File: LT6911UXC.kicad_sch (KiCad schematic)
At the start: 38 parts, among them U7 TC358743XBG_EL_NOK, U8 LX7167ACLD-TR, U9 TLV62568DBVR, X2 27MHz

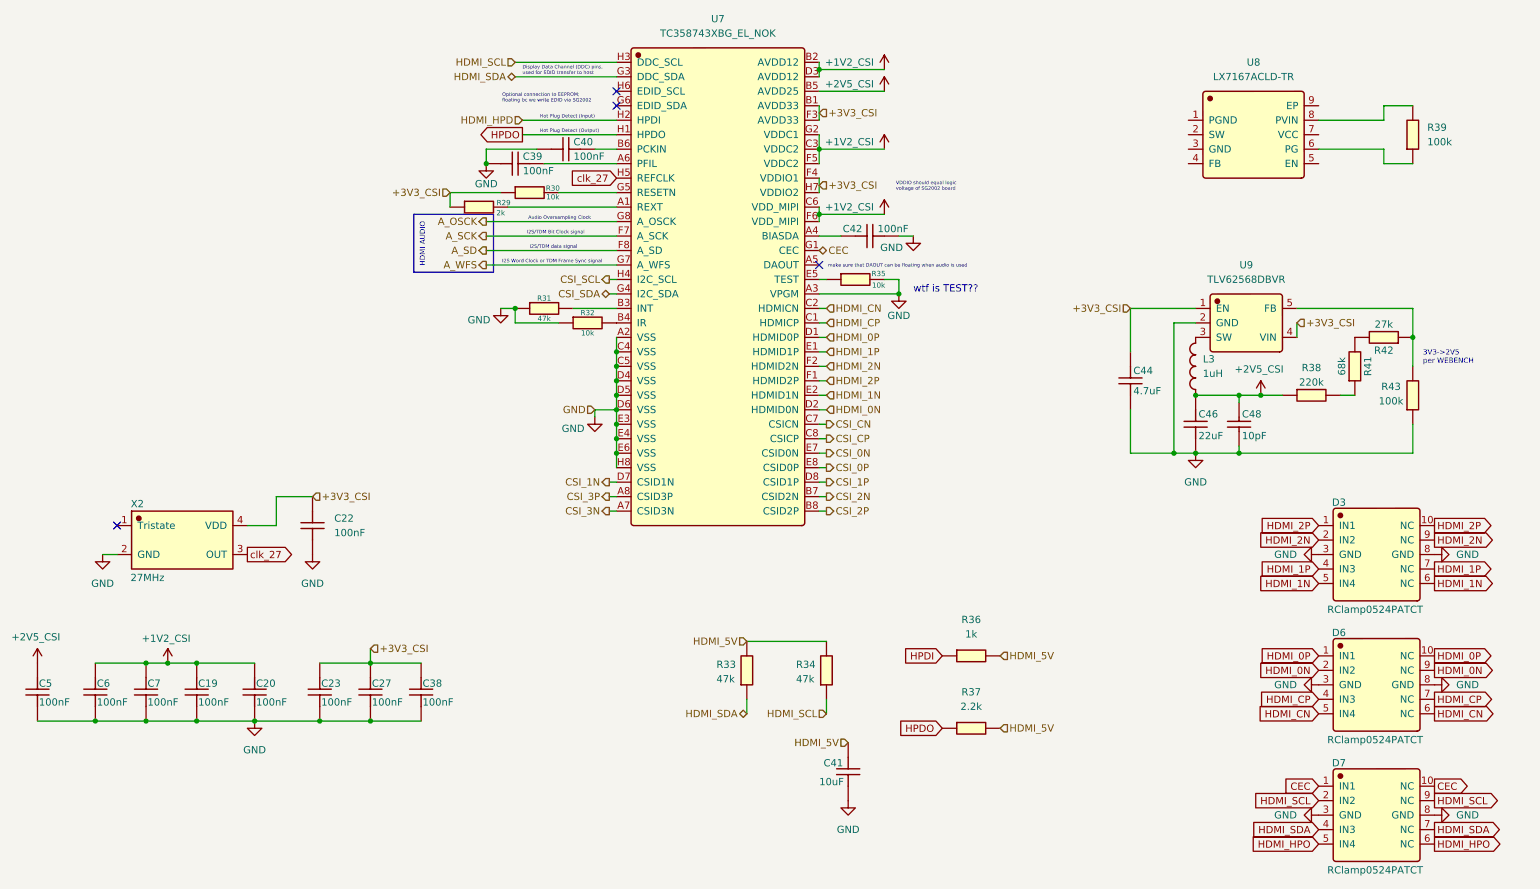
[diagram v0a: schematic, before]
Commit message: Cleaned up schematic and replaced TC358743XBG with reverse-engineered LT6911C
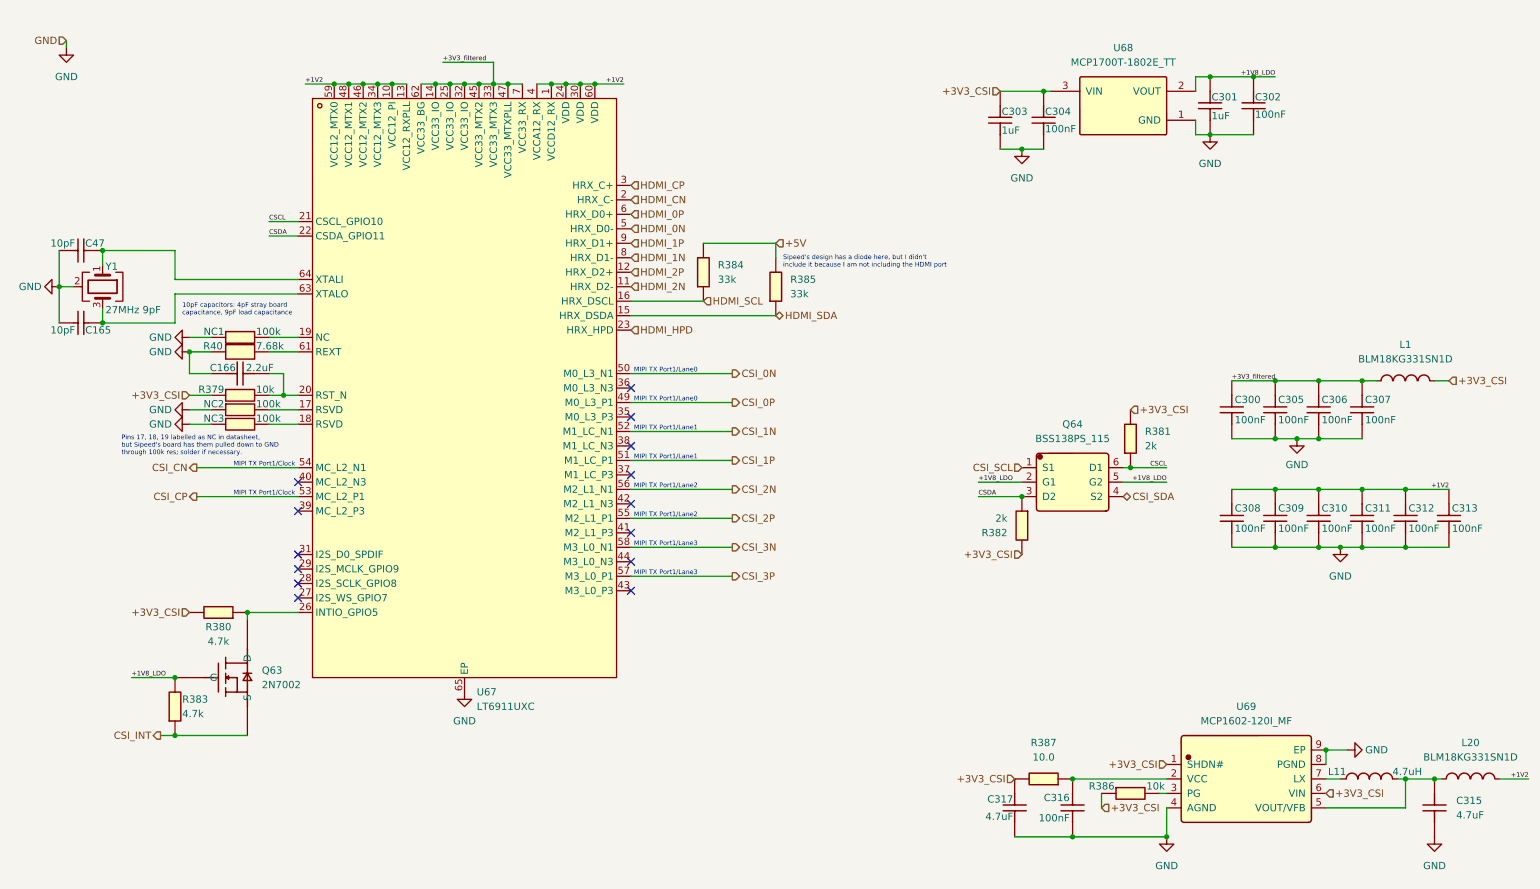
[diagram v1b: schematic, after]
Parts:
- removed C19, C20, C22, C23, C27, C38, C39, C40, C42, C5, C6, C7: 100nF, Capacitor_SMD:C_0402_1005Metric, symbol JLCImport:CL05B104KB54PNC
- removed C41: 10uF, Capacitor_SMD:C_0603_1608Metric, symbol JLCImport:CL10A106KP8NNNC
- removed C44: 4.7uF, Capacitor_SMD:C_0603_1608Metric, symbol JLCImport:CL10A475KO8NNNC
- removed C46: 22uF, Capacitor_SMD:C_0603_1608Metric, symbol JLCImport:CL10A226MQ8NRNC
- removed C48: 10pF, Capacitor_SMD:C_0603_1608Metric, symbol JLCImport:CL10C100JB8NNNC
- removed D3, D6, D7: RClamp0524PATCT, JLCImport:RClamp0524PATCT, symbol JLCImport:RClamp0524PATCT
- removed L3: 1uH, TerminalBlock_Phoenix:TerminalBlock_Phoenix_PTSM-0,5-2-2,5-V-SMD_1x02-1MP_P2.50mm_Vertical, symbol JLCImport:FTC252012S1R0MBCA
- removed R29: 2k, Resistor_SMD:R_0603_1608Metric, symbol JLCImport:0603WAF2001T5E
- removed R30, R32, R35: 10k, Resistor_SMD:R_0402_1005Metric, symbol JLCImport:0402WGF1002TCE
- removed R31, R33, R34: 47k, Resistor_SMD:R_0402_1005Metric, symbol JLCImport:0402WGF4702TCE
- removed R36: 1k, Resistor_SMD:R_0402_1005Metric, symbol JLCImport:0402WGF1001TCE
- removed R37: 2.2k, Resistor_SMD:R_0402_1005Metric, symbol JLCImport:0402WGF2201TCE
- removed R38: 220k, Resistor_SMD:R_0603_1608Metric, symbol JLCImport:0603WAF2203T5E
- removed R39, R43: 100k, Resistor_SMD:R_0402_1005Metric, symbol JLCImport:0402WGF1003TCE
- removed R41: 68k, Resistor_SMD:R_0603_1608Metric, symbol JLCImport:0603WAF6802T5E
- removed R42: 27k, Resistor_SMD:R_0603_1608Metric, symbol JLCImport:0603WAF2702T5E
- removed U7: TC358743XBG_EL_NOK, JLCImport:TC358743XBG_EL_NOK, symbol JLCImport:TC358743XBG_EL_NOK
- removed U8: LX7167ACLD-TR, JLCImport:LX7167ACLD-TR, symbol JLCImport:LX7167ACLD-TR
- removed U9: TLV62568DBVR, JLCImport:TLV62568DBVR, symbol JLCImport:TLV62568DBVR
- removed X2: 27MHz, Oscillator:Oscillator_SMD_Silicon_Labs_LGA-6_2.5x3.2mm_P1.25mm, symbol JLCImport:XOS32027000LT00351005
- added C165, C47: 10pF, Capacitor_SMD:C_0603_1608Metric, symbol JLCImport:CL10C100JB8NNNC
- added C166: 2.2uF, Capacitor_SMD:C_0402_1005Metric, symbol JLCImport:JMK105BJ225MVHF
- added C300, C302, C304, C305, C306, C307, C308, C309, C310, C311, C312, C313, C316: 100nF, Capacitor_SMD:C_0402_1005Metric, symbol JLCImport:CL05B104KB54PNC
- added C301, C303: 1uF, Capacitor_SMD:C_0402_1005Metric, symbol JLCImport:CL05A105KA5NQNC
- added C315, C317: 4.7uF, Capacitor_SMD:C_0402_1005Metric, symbol JLCImport:CL05A475MP5NRNC
- added L1, L20: BLM18KG331SN1D, JLCImport:BLM18KG331SN1D, symbol JLCImport:BLM18KG331SN1D
- added L11: 4.7uH, JLCImport:PIM201608S4R7MBCA, symbol JLCImport:PIM201608S4R7MBCA
- added NC1, NC2, NC3: 100k, Resistor_SMD:R_0402_1005Metric, symbol JLCImport:0402WGF1003TCE
- added Q63: 2N7002, JLCImport:2N7002_C916396, symbol JLCImport:2N7002_C916396
- added Q64: BSS138PS_115, JLCImport:BSS138PS_115, symbol JLCImport:BSS138PS_115
- added R379, R386: 10k, Resistor_SMD:R_0402_1005Metric, symbol JLCImport:0402WGF1002TCE
- added R380, R383: 4.7k, Resistor_SMD:R_0402_1005Metric, symbol JLCImport:0402WGF4701TCE
- added R381, R382: 2k, Resistor_SMD:R_0603_1608Metric, symbol JLCImport:0603WAF2001T5E
- added R384, R385: 33k, Resistor_SMD:R_0402_1005Metric, symbol JLCImport:WR04X3302FTL
- added R387: 10.0, Resistor_SMD:R_0402_1005Metric, symbol JLCImport:0402WGF100JTCE
- added R40: 7.68k, Resistor_SMD:R_0402_1005Metric, symbol JLCImport:CL0402FN7K68P
- added U67: LT6911UXC, LT6911UXC:QFN-64_L7.5-W7.5-P0.40-TL-EP6.2, symbol LT6911UXC:LT6911UXC
- added U68: MCP1700T-1802E_TT, JLCImport:MCP1700T-1802E_TT, symbol JLCImport:MCP1700T-1802E_TT
- added U69: MCP1602-120I_MF, JLCImport:MCP1602-120I_MF, symbol JLCImport:MCP1602-120I_MF
- added Y1: 27MHz 9pF, Crystal:Crystal_SMD_3225-4Pin_3.2x2.5mm, symbol Device:Crystal_GND24
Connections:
- net +3V3_CSI: now also C303.2, C304.2, C317.2, L1.2, R379.1, R380.2, R381.2, R382.2, R386.1, R387.2, U68.3 (VIN), U69.1 (SHDN#), U69.6 (VIN)
- net CSI_0N: now also U67.50 (M0_L3_N1)
- net CSI_0P: now also U67.49 (M0_L3_P1)
- net CSI_1N: now also U67.52 (M1_LC_N1)
- net CSI_1P: now also U67.51 (M1_LC_P1)
- net CSI_2N: now also U67.56 (M2_L1_N1)
- net CSI_2P: now also U67.55 (M2_L1_P1)
- net CSI_3N: now also U67.58 (M3_L0_N1)
- net CSI_3P: now also U67.57 (M3_L0_P1)
- net CSI_CN: now also U67.54 (MC_L2_N1)
- net CSI_CP: now also U67.53 (MC_L2_P1)
- net CSI_SCL: now also Q64.1 (S1)
- net CSI_SDA: now also Q64.4 (S2)
- net GND: now also C165.2, C166.2, C300.1, C301.1, C302.1, C303.1, C304.1, C305.1, C306.1, C307.1, C308.1, C309.1, C310.1, C311.1, C312.1, C313.1, C315.1, C316.1, C317.1, C47.1, NC1.1, NC2.1, NC3.1, R40.1, U67.65 (EP), U68.1 (GND), U69.4 (AGND), U69.8 (PGND), U69.9 (EP), Y1.2 (G), Y1.4 (G)
- net HDMI_0N: now also U67.5 (HRX_D0-)
- net HDMI_0P: now also U67.6 (HRX_D0+)
- net HDMI_1N: now also U67.8 (HRX_D1-)
- net HDMI_1P: now also U67.9 (HRX_D1+)
- net HDMI_2N: now also U67.11 (HRX_D2-)
- net HDMI_2P: now also U67.12 (HRX_D2+)
- net HDMI_CN: now also U67.2 (HRX_C-)
- net HDMI_CP: now also U67.3 (HRX_C+)
- net HDMI_HPD: now also U67.23 (HRX_HPD)
- net HDMI_SCL: now also R384.1, U67.16 (HRX_DSCL)
- net HDMI_SDA: now also R385.1, U67.15 (HRX_DSDA)
- new net: C47.2, U67.64 (XTALI), Y1.1
- new net: C316.2, R387.1, U69.2 (VCC)
- new net: R386.2, U69.3 (PG)
- new net: C315.2, L11.2, L20.1, U69.5 (VOUT/VFB)
- new net: L11.1, U69.7 (LX)
- new net: Q63.3 (D), R380.1, U67.26 (INTIO_GPIO5)
- new net: C165.1, U67.63 (XTALO), Y1.3
- new net: NC2.2, U67.17 (RSVD)
- new net: NC3.2, U67.18 (RSVD)
- new net: NC1.2, U67.19 (NC)
- new net: C166.1, R379.2, U67.20 (RST_N)
- new net: R40.2, U67.61 (REXT)
- new net +1V2: C308.2, C309.2, C310.2, C311.2, C312.2, C313.2, L20.2, U67.1 (VCCD12_RX), U67.10 (VCC12_PI), U67.13 (VCC12_RXPLL), U67.24 (VDD), U67.30 (VDD), U67.34 (VCC12_MTX3), U67.4 (VCCA12_RX), U67.46 (VCC12_MTX2), U67.48 (VCC12_MTX1), U67.59 (VCC12_MTX0), U67.60 (VDD)
- new net +1V8_LDO: C301.2, C302.2, Q63.1 (G), Q64.2 (G1), Q64.5 (G2), R383.2, U68.2 (VOUT)
- new net +3V3_filtered: C300.2, C305.2, C306.2, C307.2, L1.1, U67.14 (VCC33_IO), U67.25 (VCC33_IO), U67.32 (VCC33_IO), U67.33 (VCC33_MTX3), U67.45 (VCC33_MTX2), U67.47 (VCC33_MTXPLL), U67.62 (VCC33_BG), U67.7 (VCC33_RX)
- new net +5V: R384.2, R385.2
- new net CSCL: Q64.6 (D1), R381.1, U67.21 (CSCL_GPIO10)
- new net CSDA: Q64.3 (D2), R382.1, U67.22 (CSDA_GPIO11)
- new net CSI_INT: Q63.2 (S), R383.1
- no-connect marks 4 -> 14
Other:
- note added: "10pF capacitors: 4pF stray board capacitance, 9pF load capacitance"
- note added: "MIPI TX Port1/Clock"
- note added: "MIPI TX Port1/Lane0"
- note added: "MIPI TX Port1/Lane1"
- note added: "MIPI TX Port1/Lane2"
- note added: "MIPI TX Port1/Lane3"
- note added: "Pins 17, 18, 19 labelled as NC in datasheet, but Sipeed's board has them pulled down to GND through 100k res; solder if necessary."
- note added: "Sipeed's design has a diode here, but I didn't include it because I am not including the HDMI port"
- note removed: "3V3->2V5 per WEBENCH"
- note removed: "Audio Oversampling Clock"
- note removed: "Display Data Channel (DDC) pins, used for EDID transfer to host"
- note removed: "HDMI AUDIO"
- note removed: "Hot Plug Detect (Input)"
- note removed: "Hot Plug Detect (Output)"
- note removed: "I2S Word Clock or TDM Frame Sync signal"
- note removed: "I2S/TDM Bit Clock signal"
- note removed: "I2S/TDM data signal"
- note removed: "Optional connection to EEPROM; floating bc we write EDID via SG2002"
- note removed: "VDDIO should equal logic voltage of SG2002 board"
- note removed: "make sure that DAOUT can be floating when audio is used"
- note removed: "wtf is TEST??"
- company: Matthew Kong -> (none)
- title: Custom HDMI->CSI for SG2002 IPKVM -> (none)

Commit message: Basic Function Review and Documentation for TUSB1064 subsystem
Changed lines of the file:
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@@
 	)
 	(hierarchical_label "HDMI_HPD"
-		(shape input)
+		(shape output)
 		(at 123.19 68.58 0)
 		(effects

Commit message: Small bug fixes to LT6911C subsystem to match official adapter model
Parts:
- removed C302, C304: 100nF, Capacitor_SMD:C_0402_1005Metric, symbol JLCImport:CL05B104KB54PNC
- removed L1, L20: BLM18KG331SN1D, JLCImport:BLM18KG331SN1D, symbol JLCImport:BLM18KG331SN1D
- removed Q64: BSS138PS_115, JLCImport:BSS138PS_115, symbol JLCImport:BSS138PS_115
- added C137, C147, C7: 10uF, Capacitor_SMD:C_0402_1005Metric, symbol JLCImport:CL05A106MQ5NUNC
- added DNP2, DNP3: 10k, Resistor_SMD:R_0402_1005Metric, symbol Device:R
- added L19, L3: 120Ω@100MHz, Inductor_SMD:L_0805_2012Metric, symbol JLCImport:GDPZ2012M121-4A0TF
- added Q65: EM6K7T2R, JLCImport:EM6K7T2R, symbol JLCImport:EM6K7T2R
- added R62: 1M, Resistor_SMD:R_0402_1005Metric, symbol JLCImport:0402WGF1004TCE
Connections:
- net +1V2: now also C166.2, C137.2, C7.2, L3.2
- net +1V8_LDO: now also DNP2.2, DNP3.2, Q65.2 (G1), Q65.5 (G2)
- net +3V3_CSI: now also L19.2
- net +3V3_filtered: now also C147.2, L19.1
- net CSCL: now also Q65.6 (D1)
- net CSDA: now also Q65.3 (D2)
- net CSI_SCL: now also DNP3.1, Q65.1 (S1)
- net CSI_SDA: now also DNP2.1, Q65.4 (S2)
- net GND: now also C166.1, C137.1, C147.1, C7.1; no longer C166.2
- net at C47.2, U67.64 (XTALI), Y1.1: now also R62.2
- net at C315.2, L11.2, U69.5 (VOUT/VFB): now also L3.1
- net at C165.1, U67.63 (XTALO), Y1.3: now also R62.1
- net at R379.2, U67.20 (RST_N): no longer C166.1
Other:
- company: (none) -> Designed By: Matthew Kong
- title: (none) -> LT6911C HDMI->MIPI CSI Subsystem
- moved on the sheet: C165, C300, C303, C305, C306, C307, C47, R381, R382, Y1

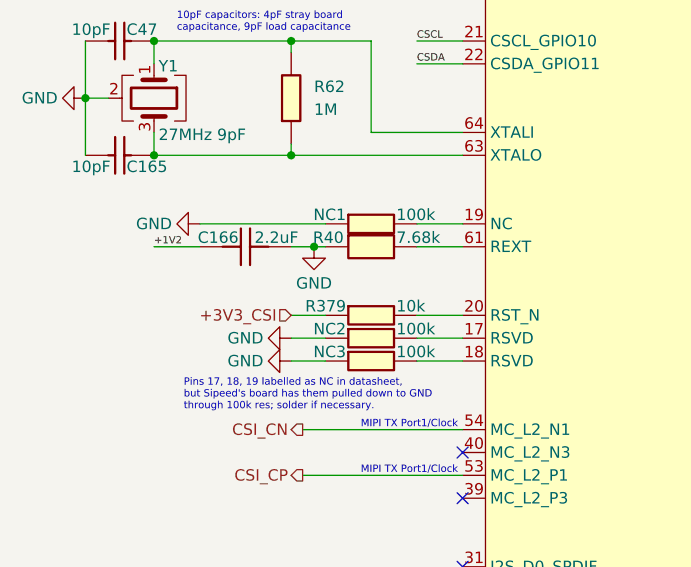
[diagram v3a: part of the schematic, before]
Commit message: Updated LT6911C docs
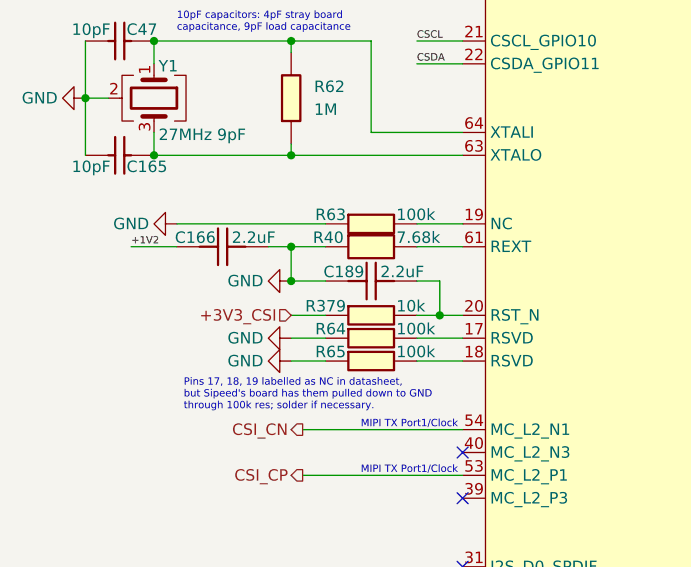
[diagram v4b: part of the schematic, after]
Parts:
- removed NC1, NC2, NC3: 100k, Resistor_SMD:R_0402_1005Metric, symbol JLCImport:0402WGF1003TCE
- added C189: 2.2uF, Capacitor_SMD:C_0402_1005Metric, symbol JLCImport:JMK105BJ225MVHF
- added R63, R64, R65: 100k, Resistor_SMD:R_0402_1005Metric, symbol JLCImport:0402WGF1003TCE
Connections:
- net GND: now also C189.2, R63.1, R64.1, R65.1
- net at U67.17 (RSVD): now also R64.2
- net at U67.18 (RSVD): now also R65.2
- net at U67.19 (NC): now also R63.2
- net at R379.2, U67.20 (RST_N): now also C189.1
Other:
- moved on the sheet: C166

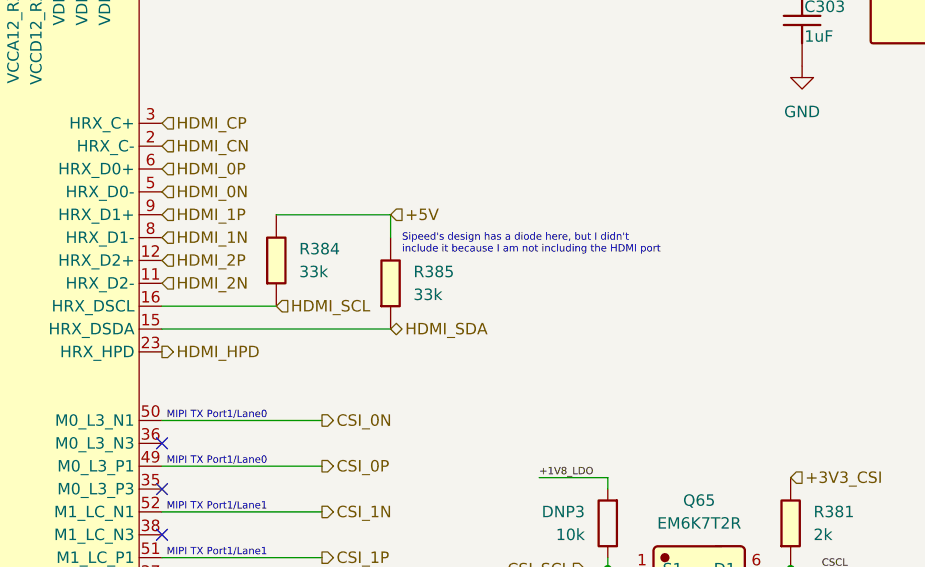
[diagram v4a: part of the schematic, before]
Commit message: Basic Function Review/Documentation for LT6911C Subsystem
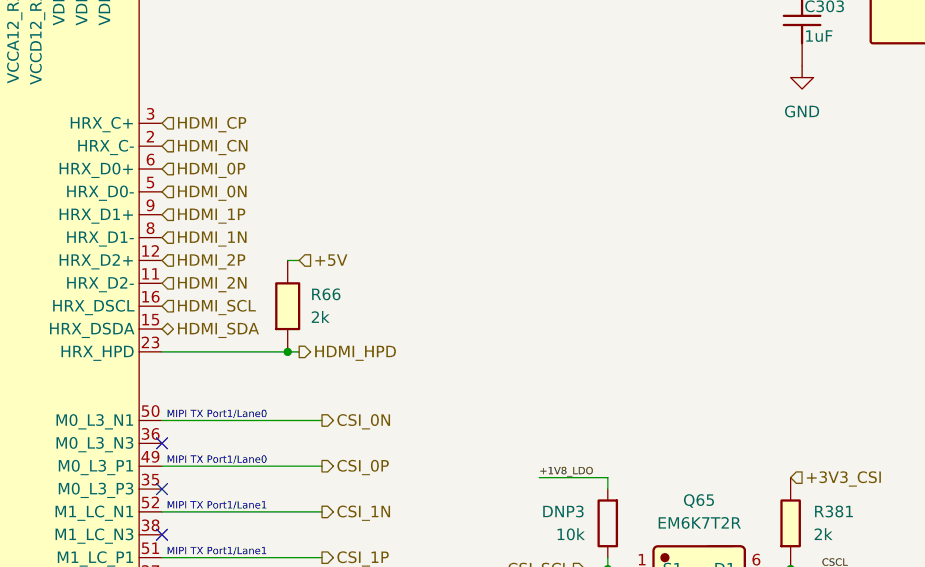
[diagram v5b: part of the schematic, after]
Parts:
- removed R384, R385: 33k, Resistor_SMD:R_0402_1005Metric, symbol JLCImport:WR04X3302FTL
- added R66: 2k, Resistor_SMD:R_0402_1005Metric, symbol JLCImport:1RC0402J0202
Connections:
- net +5V: now also R66.2
- net HDMI_HPD: now also R66.1
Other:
- note removed: "Sipeed's design has a diode here, but I didn't include it because I am not including the HDMI port"
